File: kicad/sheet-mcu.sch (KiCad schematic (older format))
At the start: 36 parts, among them SW1 SW_Push, SW2 SW_Push, SW3 SW_Push, U14 TJA1051T-3, U15 STM32F405RGTx

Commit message: layout and bom complete - waiting on parts from jlcpcb
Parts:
- C45, C46: value 12pf -> 12p
- C47, C50: footprint (none) -> Capacitor_SMD:C_0603_1608Metric
- C51, C52: value 2.2uf -> 2.2u; footprint Capacitor_SMD:C_0603_1608Metric_Pad1.08x0.95mm_HandSolder -> Capacitor_SMD:C_0603_1608Metric
- C53, C55: value 10nF -> 10n; footprint (none) -> Capacitor_SMD:C_0402_1005Metric
- C54: value 10uF -> 10u; footprint (none) -> Capacitor_SMD:C_0603_1608Metric
- R51: value 36K -> 33K
- R52, R54: footprint (none) -> Resistor_SMD:R_0402_1005Metric
- R56, R57, R58: footprint Resistor_SMD:R_0603_1608Metric -> Resistor_SMD:R_0402_1005Metric
- SW1, SW2, SW3: value SW_Push -> push; footprint (none) -> Button_Switch_SMD:SW_Push_SPST_NO_Alps_SKRK
- TH1, TH2: footprint (none) -> Resistor_SMD:R_0603_1608Metric
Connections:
- net GND: now also R55.2; no longer R55.1
- net USER_BUTTON: now also R55.1; no longer R55.2
- net HALL_U_I2C_1_SCL renamed I2C_1_SCL
- net HALL_V_I2C_1_SDA renamed I2C_1_SDA
- net USART2_RX renamed HALL_V_1
- net USART2_TX renamed HALL_U_1
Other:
- moved on the sheet: C48, R49, SW1

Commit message: Adding 0.9 version
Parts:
- removed C53, C55: 10n, Capacitor_SMD:C_0402_1005Metric, symbol Device:C_Small
- removed R52, R54: 4k7, Resistor_SMD:R_0402_1005Metric, symbol Device:R_Small
- removed TH1, TH2: Thermistor, Resistor_SMD:R_0603_1608Metric, symbol Device:Thermistor
- R14: renamed from R50; value 220 -> 120R+; footprint Resistor_SMD:R_0402_1005Metric -> Resistor_SMD:R_1206_3216Metric
- renumbered C45 to C16, C46 to C17, C48 to C18, C47 to C19, C49 to C20, C50 to C21, C51 to C22, C52 to C23, C54 to C24, C56 to C25, D8 to D2, D9 to D3, D10 to D4, R46 to R10, R47 to R11, R48 to R12, R49 to R13, R51 to R15, R53 to R16, R55 to R17, R56 to R18, R57 to R19, R58 to R20, U14 to U2, U15 to U3
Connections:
- net HALL_U_1 renamed HALL_U1
- net HALL_U_I2C_2_SCL renamed HALL_U2
- net HALL_V_1 renamed HALL_V1
- net HALL_V_I2C_2_SDA renamed HALL_V2
- net HALL_W_1 renamed HALL_W1
- net HALL_W_2 renamed HALL_W2
- net HIN_U_1 renamed IN_U1
- net HIN_U_2 renamed IN_U2
- net HIN_V_1 renamed IN_V1
- net HIN_V_2 renamed IN_V2
- net HIN_W_1 renamed IN_W1
- net HIN_W_2 renamed IN_W2
- net I2C_1_SCL renamed I2C1_SCL
- net I2C_1_SDA renamed I2C1_SDA
- net JTAG_DI renamed SENSE_W1
- net JTAG_DO renamed SWO
- net LIN_U_1 renamed EN_U1
- net LIN_U_2 renamed EN_U2
- net LIN_V_1 renamed EN_V1
- net LIN_V_2 renamed EN_V2
- net LIN_W_1 renamed EN_W1
- net LIN_W_2 renamed EN_W2
- net SENSE_U_1 renamed SENSE_U1
- net SENSE_U_2 renamed SENSE_U2
- net SENSE_V_1 renamed SENSE_V1
- net SENSE_V_2 renamed SENSE_V2
- net SENSE_W_1 renamed MPU_INT
- net SENSE_W_2 renamed SENSE_W2
- net SERVO: no longer names the net of U3.4 (PC15)
- net TEMP_1: no longer names the net of U3.11 (PC3)
- net TEMP_2: no longer names the net of U3.24 (PC4)
- no-connect marks 0 -> 3
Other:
- note removed: "TEMPERATURE"

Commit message: updating bom and pos files
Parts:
- R18, R19, R20: value 1K -> 1k
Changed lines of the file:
@@
 AR Path="/6027096C/602D028C" Ref="R19"  Part="1"
 F 0 "R19" H 4391 7254 50  0000 R CNN
-F 1 "1K" H 4391 7345 50  0000 R CNN
+F 1 "1k" H 4391 7345 50  0000 R CNN
 F 2 "Resistor_SMD:R_0402_1005Metric" H 4450 7300 50  0001 C CNN
 F 3 "~" H 4450 7300 50  0001 C CNN
@@
 AR Path="/6027096C/602D02B0" Ref="R18"  Part="1"
 F 0 "R18" H 4141 7254 50  0000 R CNN
-F 1 "1K" H 4141 7345 50  0000 R CNN
+F 1 "1k" H 4141 7345 50  0000 R CNN
 F 2 "Resistor_SMD:R_0402_1005Metric" H 4200 7300 50  0001 C CNN
 F 3 "~" H 4200 7300 50  0001 C CNN
@@
 AR Path="/6027096C/602D029E" Ref="R20"  Part="1"
 F 0 "R20" H 4641 7254 50  0000 R CNN
-F 1 "1K" H 4641 7345 50  0000 R CNN
+F 1 "1k" H 4641 7345 50  0000 R CNN
 F 2 "Resistor_SMD:R_0402_1005Metric" H 4700 7300 50  0001 C CNN
 F 3 "~" H 4700 7300 50  0001 C CNN

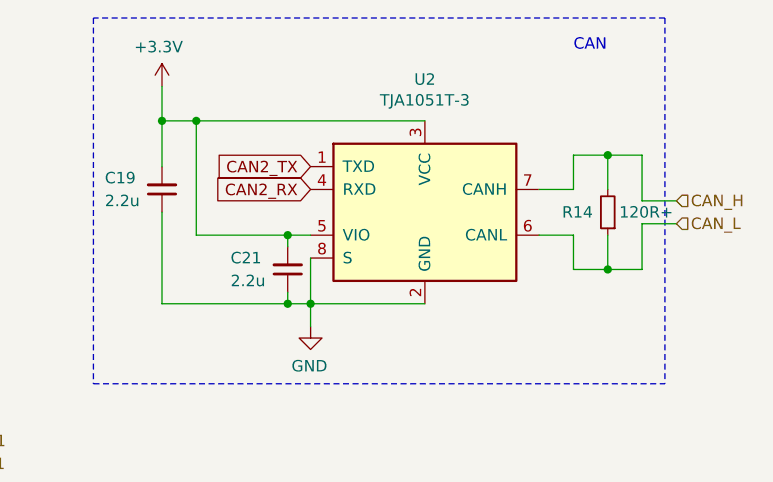
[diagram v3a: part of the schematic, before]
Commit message: v0.9.1 swapping can to 3.3v SN65HVD230
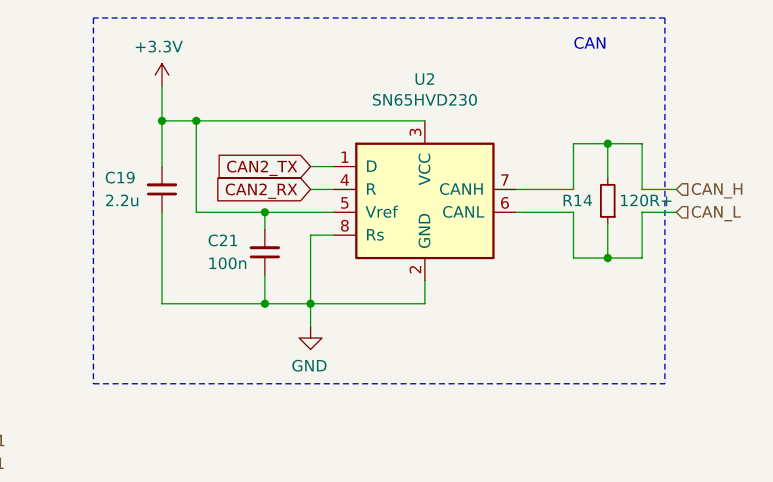
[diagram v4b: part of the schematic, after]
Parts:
- removed U2: TJA1051T-3, Package_SO:SOIC-8_3.9x4.9mm_P1.27mm, symbol Interface_CAN_LIN:TJA1051T-3
- added U2: SN65HVD230, Package_SO:SOIC-8_3.9x4.9mm_P1.27mm, symbol Interface_CAN_LIN:SN65HVD230
- C21: value 2.2u -> 100n; footprint Capacitor_SMD:C_0603_1608Metric -> Capacitor_SMD:C_0402_1005Metric
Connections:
- net +3V3: now also U2.3 (VCC), U2.5 (Vref)
- net CAN2_RX: now also U2.4 (R)
- net CAN2_TX: now also U2.1 (D)
- net CAN_H: now also U2.7 (CANH)
- net CAN_L: now also U2.6 (CANL)
- net GND: now also U2.2 (GND), U2.8 (Rs)
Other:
- moved on the sheet: C21, R14
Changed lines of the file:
@@
 	1    0    0    -1
 $EndComp
-$Comp
-L Interface_CAN_LIN:TJA1051T-3 U?
-U 1 1 60335B5F
-P 9300 1400
-AR Path="/60335B5F" Ref="U?"  Part="1"
-AR Path="/6027096C/60335B5F" Ref="U2"  Part="1"
-F 0 "U2" H 9300 1981 50  0000 C CNN
-F 1 "TJA1051T-3" H 9300 1890 50  0000 C CNN
-F 2 "Package_SO:SOIC-8_3.9x4.9mm_P1.27mm" H 9300 900 50  0001 C CIN
-F 3 "http://www.nxp.com/documents/data_sheet/TJA1051.pdf" H 9300 1400 50  0001 C CNN
-	1    9300 1400
-	1    0    0    -1
-$EndComp
-Wire Wire Line
-	10400 1350 10250 1350
-Wire Wire Line
-	10250 1350 10250 1150
+Wire Wire Line
+	10400 1300 10250 1300
+Wire Wire Line
+	10250 1300 10250 1100
 $Comp
 L Device:R_Small R?
 U 1 1 60335B67
-P 10100 1400
+P 10100 1350
 AR Path="/60335B67" Ref="R?"  Part="1"
 AR Path="/6027096C/60335B67" Ref="R14"  Part="1"
-F 0 "R14" H 10300 1400 50  0000 R CNN
-F 1 "120R+" H 10050 1400 50  0000 R CNN
-F 2 "Resistor_SMD:R_1206_3216Metric" H 10100 1400 50  0001 C CNN
-F 3 "~" H 10100 1400 50  0001 C CNN
-	1    10100 1400
+F 0 "R14" H 10300 1350 50  0000 R CNN
+F 1 "120R+" H 10050 1350 50  0000 R CNN
+F 2 "Resistor_SMD:R_1206_3216Metric" H 10100 1350 50  0001 C CNN
+F 3 "~" H 10100 1350 50  0001 C CNN
+	1    10100 1350
 	-1   0    0    1
 $EndComp
 Wire Wire Line
-	9800 1300 9950 1300
-Wire Wire Line
-	9950 1300 9950 1150
-Wire Wire Line
-	9950 1150 10100 1150
-Wire Wire Line
-	9800 1500 9950 1500
-Wire Wire Line
-	9950 1500 9950 1650
-Wire Wire Line
-	9950 1650 10100 1650
-Wire Wire Line
-	10100 1500 10100 1650
-Connection ~ 10100 1650
-Wire Wire Line
-	10100 1650 10250 1650
-Wire Wire Line
-	10100 1300 10100 1150
-Connection ~ 10100 1150
-Wire Wire Line
-	10100 1150 10250 1150
-Wire Wire Line
-	10250 1450 10400 1450
-Wire Wire Line
-	10250 1450 10250 1650
+	9950 1100 10100 1100
+Wire Wire Line
+	9950 1600 10100 1600
+Wire Wire Line
+	10100 1450 10100 1600
+Connection ~ 10100 1600
+Wire Wire Line
+	10100 1600 10250 1600
+Wire Wire Line
+	10100 1250 10100 1100
+Connection ~ 10100 1100
+Wire Wire Line
+	10100 1100 10250 1100
+Wire Wire Line
+	10250 1400 10400 1400
+Wire Wire Line
+	10250 1400 10250 1600
 Text GLabel 8800 1300 0    50   Input ~ 0
 CAN2_RX
@@
 Wire Wire Line
 	8800 1800 9300 1800
-Wire Wire Line
-	8800 1800 8800 1600
 $Comp
 L Device:C_Small C?
 U 1 1 60335B93
-P 8700 1650
+P 8600 1575
 AR Path="/60335B93" Ref="C?"  Part="1"
 AR Path="/6027096C/60335B93" Ref="C21"  Part="1"
-F 0 "C21" H 8950 1600 50  0000 R CNN
-F 1 "2.2u" H 8950 1700 50  0000 R CNN
-F 2 "Capacitor_SMD:C_0603_1608Metric" H 8700 1650 50  0001 C CNN
-F 3 "~" H 8700 1650 50  0001 C CNN
-	1    8700 1650
+F 0 "C21" H 8850 1525 50  0000 R CNN
+F 1 "100n" H 8850 1625 50  0000 R CNN
+F 2 "Capacitor_SMD:C_0402_1005Metric" H 8600 1575 50  0001 C CNN
+F 3 "~" H 8600 1575 50  0001 C CNN
+	1    8600 1575
 	-1   0    0    1
 $EndComp
-Wire Wire Line
-	8700 1550 8700 1500
-Wire Wire Line
-	8700 1500 8800 1500
-Wire Wire Line
-	8700 1750 8700 1800
-Connection ~ 8700 1800
-Wire Wire Line
-	8700 1800 8800 1800
+Connection ~ 8600 1800
 Wire Wire Line
 	8150 850  8150 1000
@@
 	8150 1000 8300 1000
 Wire Wire Line
-	8150 1800 8700 1800
-Connection ~ 8700 1500
+	8150 1800 8600 1800
 Wire Wire Line
 	8150 1400 8150 1800
@@
 	8150 1200 8150 1000
 Connection ~ 8150 1000
-Wire Wire Line
-	8300 1500 8300 1000
-Wire Wire Line
-	8300 1500 8700 1500
 Connection ~ 8300 1000
 Wire Wire Line
@@
 Wire Wire Line
 	6050 4800 7050 4800
-Text HLabel 10400 1350 2    50   Input ~ 0
+Text HLabel 10400 1300 2    50   Input ~ 0
 CAN_H
-Text HLabel 10400 1450 2    50   Input ~ 0
+Text HLabel 10400 1400 2    50   Input ~ 0
 CAN_L
 Text HLabel 7050 5500 2    50   Input ~ 0
@@
 	1    0    0    -1
 $EndComp
+$Comp
+L Interface_CAN_LIN:SN65HVD230 U2
+U 1 1 60289FE0
+P 9300 1300
+F 0 "U2" H 9300 1781 50  0000 C CNN
+F 1 "SN65HVD230" H 9300 1690 50  0000 C CNN
+F 2 "Package_SO:SOIC-8_3.9x4.9mm_P1.27mm" H 9300 800 50  0001 C CNN
+F 3 "http://www.ti.com/lit/ds/symlink/sn65hvd230.pdf" H 9200 1700 50  0001 C CNN
+	1    9300 1300
+	1    0    0    -1
+$EndComp
+Wire Wire Line
+	9300 1700 9300 1800
+Wire Wire Line
+	8600 1800 8800 1800
+Wire Wire Line
+	8800 1500 8900 1500
+Wire Wire Line
+	8800 1500 8800 1800
+Wire Wire Line
+	9700 1300 9950 1300
+Wire Wire Line
+	9950 1100 9950 1300
+Wire Wire Line
+	9700 1400 9950 1400
+Wire Wire Line
+	9950 1400 9950 1600
+Wire Wire Line
+	8300 1400 8300 1000
+Wire Wire Line
+	8600 1675 8600 1800
+Wire Wire Line
+	8300 1400 8600 1400
+Wire Wire Line
+	8600 1475 8600 1400
+Connection ~ 8600 1400
+Wire Wire Line
+	8600 1400 8900 1400
+Wire Wire Line
+	8800 1200 8900 1200
+Wire Wire Line
+	8800 1300 8900 1300
 $EndSCHEMATC
